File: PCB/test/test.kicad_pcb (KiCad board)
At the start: 2 copper layers, 64.1 x 42 mm, 174 parts, among them U1 STM32WBxx_QFN48, U2 USBLC6-2SC6, U3 LD3985M33R, U4 SFH_7072, X1 NX2016_32MHz, X2 NX2012_32K768Hz

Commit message: ajout alim TSU104
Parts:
- removed the ? at (159.2, 106.1)
- removed the ? at (162.4, 89.5)
- removed the ? at (165.3, 94.5)
- removed the ? at (170.0, 90.9)
- removed the ? at (156.3, 94.9)
- added ?: , , F.Cu at (167.5, 89.2)
- added ?: , , F.Cu at (162.3, 105.3)
- moved R11 4.28 mm to (162.2, 94.5), turned to -90 degrees
- moved R5 3.90 mm to (159.5, 89.6)
- moved ? 2.38 mm to (163.8, 101.0)
- moved ? 2.24 mm to (159.2, 105.8)
- moved R6 1.85 mm to (161.3, 90.6)
- moved ? 1.30 mm to (167.5, 90.9)
- moved C42 1.21 mm to (159.7, 93.5)
- moved R12 1.12 mm to (174.7, 101.6), turned to 0 degrees
- moved C43 0.85 mm to (161.3, 92.0)
- moved ? 0.11 mm to (156.3, 109.0)
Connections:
- TSU1 pad 1: (no net) -> Net-(C43-Pad2)
- TSU1 pad 11: (no net) -> GND
- TSU1 pad 2: (no net) -> Net-(C43-Pad1)
- TSU1 pad 3: (no net) -> GND
- TSU1 pad 4: (no net) -> 3V3
- TSU1 pad 5: GND -> (no net)
- TSU1 pad 6: Net-(C43-Pad1) -> (no net)
- TSU1 pad 7: Net-(C43-Pad2) -> (no net)
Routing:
- net Net-(C43-Pad1): track 13.9 -> 19.2 mm
- net PA4: track 29.4 -> 33.4 mm
- net PA5: track 52.3 -> 53.9 mm
- net GND: track 13.1 -> 11.5 mm
- net 3V3: track 157.2 -> 156.1 mm, vias 12 -> 13

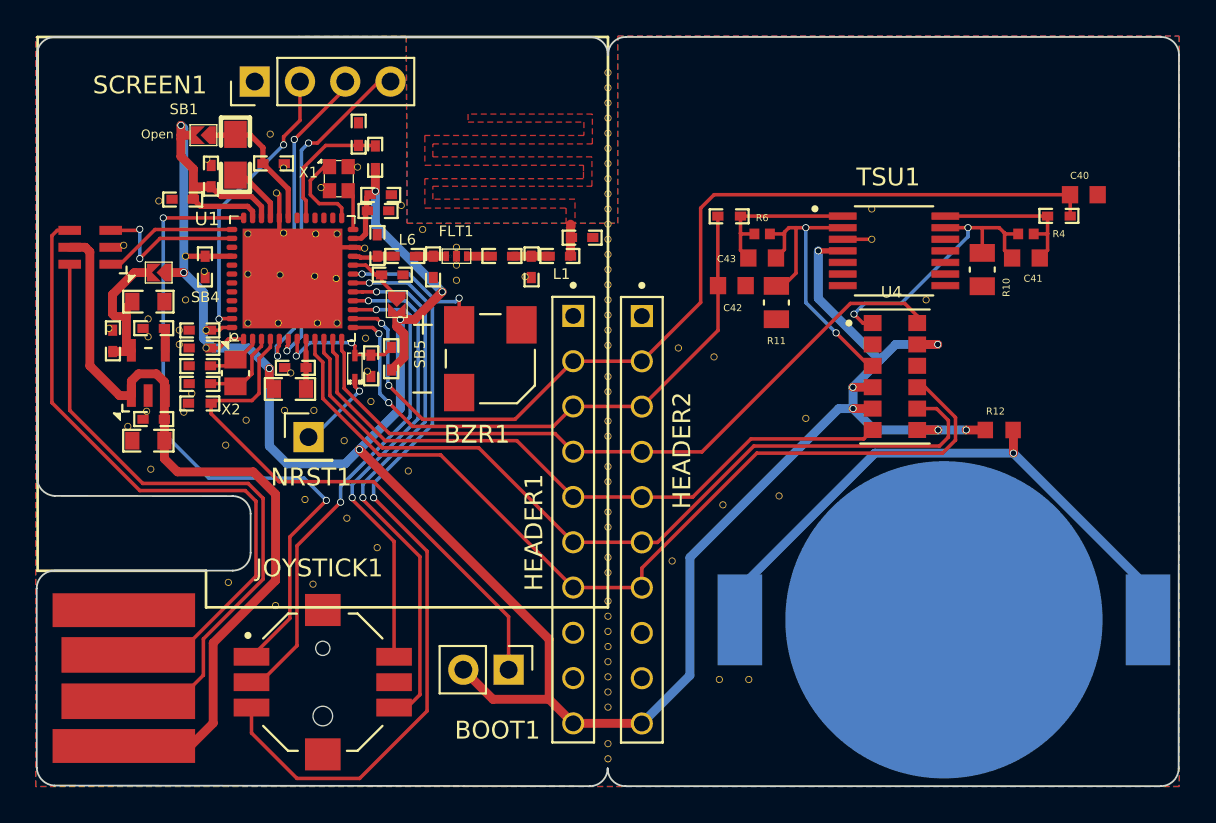
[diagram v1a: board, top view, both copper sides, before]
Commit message: ajout i2c
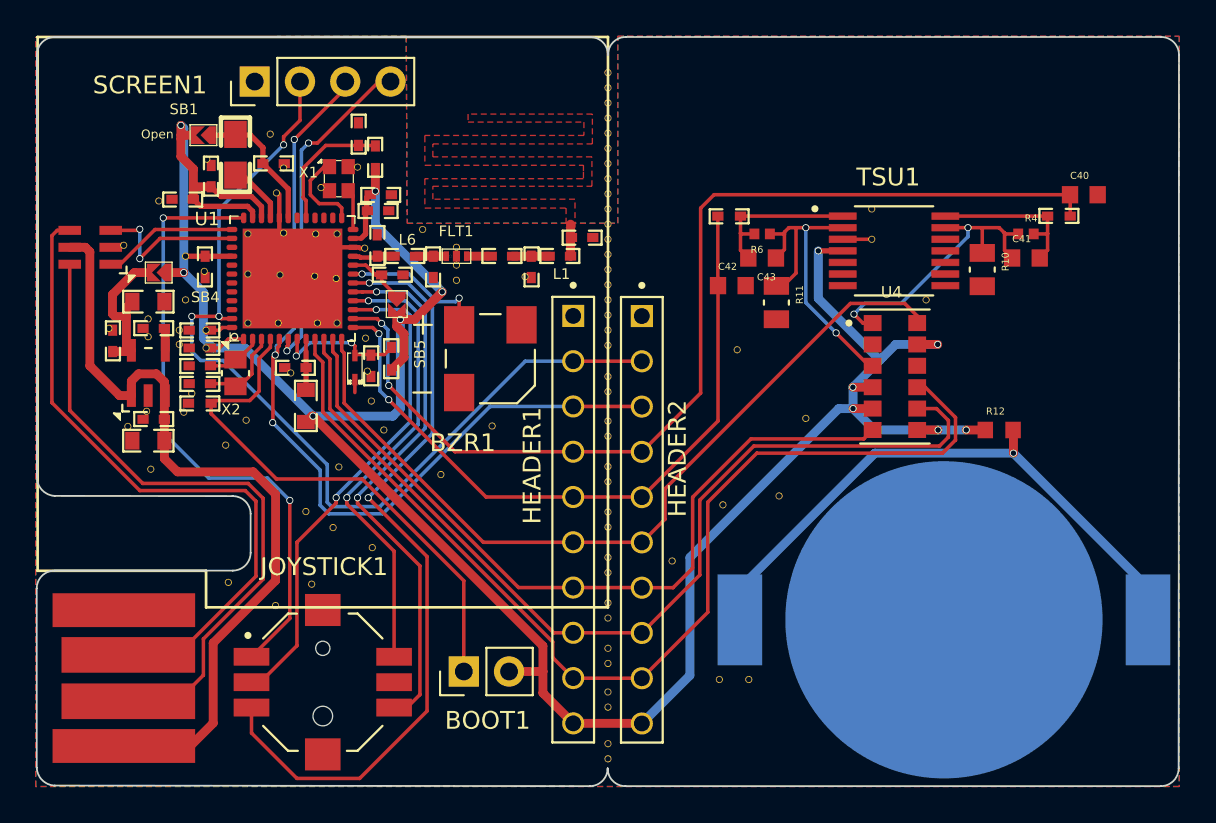
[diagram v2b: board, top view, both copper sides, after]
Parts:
- removed the ? at (137.9, 102.2)
- removed the ? at (136.2, 100.5)
- removed the ? at (152.7, 112.9)
- removed the ? at (141.1, 89.0)
- removed the ? at (134.6, 100.5)
- removed the ? at (152.7, 115.5)
- removed the ? at (141.5, 103.9)
- removed the ? at (156.7, 97.0)
- removed NRST1: Conn_01x01_Female, Connector_PinHeader_2.54mm:PinHeader_1x01_P2.54mm_Vertical
- added ?: , , F.Cu at (140.1, 101.6)
- added ?: , , F.Cu at (146.2, 101.4)
- added ?: , , F.Cu at (137.6, 103.7)
- added ?: , , F.Cu at (143.3, 104.1)
- moved BOOT1 2.52 mm to (144.6, 115.2), turned to 90 degrees
- moved ? 1.36 mm to (159.9, 97.1)
- moved L3 1.30 mm to (135.8, 100.2), turned to 90 degrees
- moved ? 0.94 mm to (137.3, 107.1)
- moved ? 0.68 mm to (135.8, 106.2)
- moved ? 0.28 mm to (139.5, 108.2)
- moved ? 0.10 mm to (152.7, 114.7)
- moved ? 0.10 mm to (152.7, 112.2)
- moved ? 0.10 mm to (152.7, 111.3)
- moved ? 0.10 mm to (152.7, 113.8)
- moved ? 0.08 mm to (136.1, 110.2)
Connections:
- HEADER1 pad 2: PA5 -> I2C_SDA
- HEADER1 pad 3: PA4 -> I2C_SCL
- HEADER1 pad 4: PA3 -> PA5
- HEADER1 pad 5: PA2 -> PA4
- HEADER1 pad 6: PA1 -> PA3
- HEADER1 pad 7: PA0 -> PA2
- HEADER1 pad 8: unconnected-(HEADER1-Pad8) -> PA1
- HEADER1 pad 9: unconnected-(HEADER1-Pad9) -> PA0
- HEADER2 pad 2: PA5 -> I2C_SDA
- HEADER2 pad 3: PA4 -> I2C_SCL
- HEADER2 pad 4: PA3 -> PA5
- HEADER2 pad 5: PA2 -> PA4
- HEADER2 pad 6: PA1 -> PA3
- HEADER2 pad 7: PA0 -> PA2
- HEADER2 pad 8: unconnected-(HEADER2-Pad8) -> PA1
- HEADER2 pad 9: unconnected-(HEADER2-Pad9) -> PA0
- SCREEN1 pad 2: Net-(SCREEN1-Pad2) -> I2C_SDA
- SCREEN1 pad 3: Net-(SCREEN1-Pad3) -> I2C_SCL
- U1 pad 47: Net-(SCREEN1-Pad2) -> I2C_SDA
- U1 pad 5: Net-(SCREEN1-Pad3) -> I2C_SCL
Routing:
- net I2C_SDA: track 0.00 -> 52.8 mm, vias 0 -> 3
- net I2C_SCL: track 0.00 -> 48.3 mm, vias 0 -> 3
- net Net-(SCREEN1-Pad3): track 18.0 -> 0.00 mm, vias 2 -> 0
- net Net-(SCREEN1-Pad2): track 15.9 -> 0.00 mm, vias 2 -> 0
- net PA0: track 51.6 -> 59.7 mm
- net PA1: track 46.8 -> 53.9 mm
- net PA2: track 37.1 -> 44.1 mm
- net PA4: track 33.4 -> 39.5 mm
- net 3V3: track 156.1 -> 150.0 mm, vias 13 -> 12
- net PA3: track 40.6 -> 46.3 mm
- net PA5: track 53.9 -> 58.4 mm
- net NRST: track 4.68 -> 0.72 mm, vias 1 -> 0
- net PA10: track 37.8 -> 34.9 mm
- net Net-(BOOT1-Pad1): track 31.2 -> 29.9 mm

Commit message: ajout 4 trous
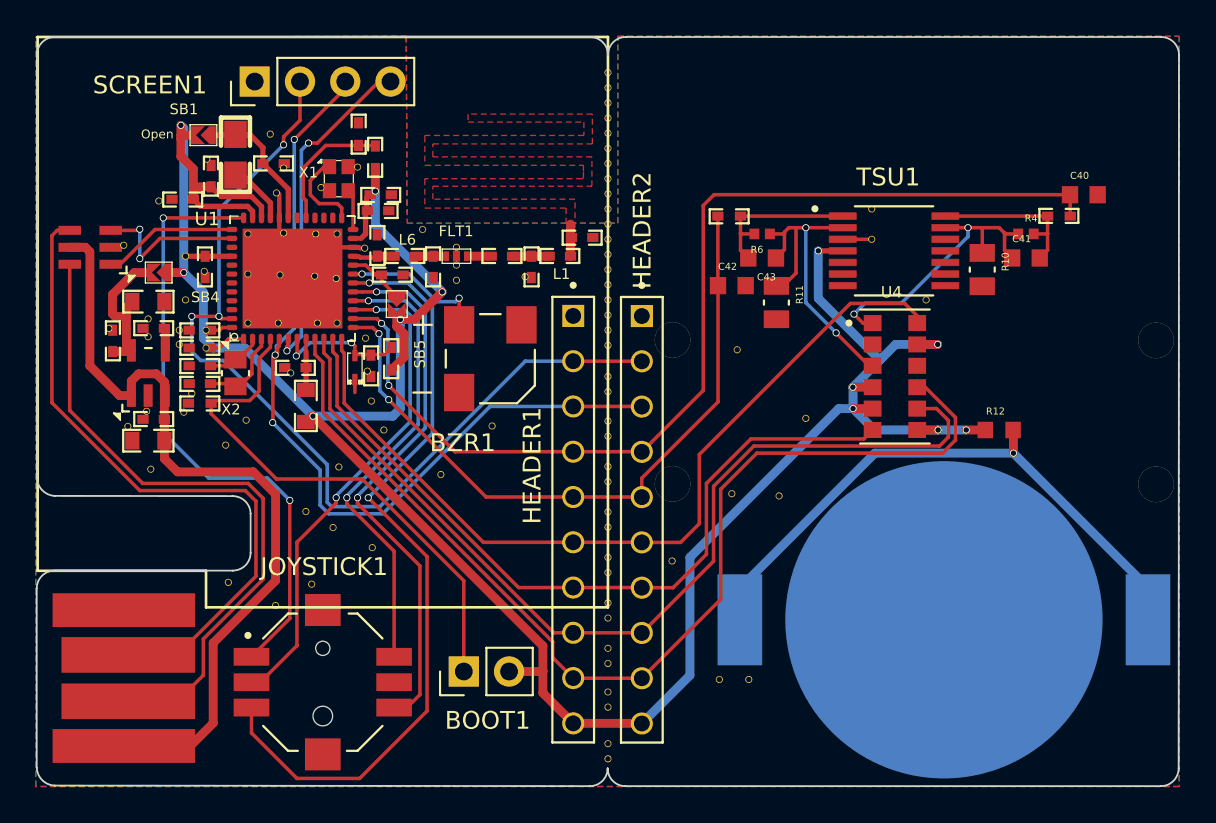
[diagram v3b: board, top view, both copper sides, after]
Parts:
- added ?: , , F.Cu at (183.4, 96.6)
- added ?: , , F.Cu at (156.3, 104.6)
- added ?: , , F.Cu at (156.3, 96.5)
- added ?: , , F.Cu at (183.4, 104.7)
- moved ? 0.80 mm to (159.7, 105.2)
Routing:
- net PA3: track 46.3 -> 47.6 mm

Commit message: améliorations pcb
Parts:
- added ?: , , F.Cu at (143.2, 109.8)
- added ?: , , F.Cu at (148.1, 119.2)
- added ?: , , F.Cu at (157.2, 95.1)
- added ?: , , F.Cu at (182.2, 85.1)
- added ?: , , F.Cu at (140.0, 90.0)
- added ?: , , F.Cu at (133.6, 118.3)
- added ?: , , F.Cu at (122.8, 82.2)
- added ?: , , F.Cu at (146.9, 108.6)
- added ?: , , F.Cu at (178.2, 90.7)
- added ?: , , F.Cu at (143.6, 97.9)
- added ?: , , F.Cu at (157.9, 119.2)
- added ?: , , F.Cu at (135.2, 91.8)
- added ?: , , F.Cu at (135.3, 95.6)
- added ?: , , F.Cu at (133.4, 91.7)
- added ?: , , F.Cu at (125.8, 83.7)
- added ?: , , F.Cu at (125.9, 89.6)
- added ?: , , F.Cu at (149.6, 120.3)
- added ?: , , F.Cu at (143.6, 101.1)
- added ?: , , F.Cu at (140.6, 87.8)
- added ?: , , F.Cu at (134.0, 83.0)
- added ?: , , F.Cu at (131.8, 118.3)
- added ?: , , F.Cu at (171.4, 82.7)
- added ?: , , F.Cu at (166.0, 101.4)
- added ?: , , F.Cu at (159.7, 94.8)
- added ?: , , F.Cu at (145.1, 103.5)
- added ?: , , F.Cu at (130.1, 102.4)
- added ?: , , F.Cu at (123.1, 102.8)
- added ?: , , F.Cu at (136.0, 102.2)
- added ?: , , F.Cu at (165.4, 103.7)
- added ?: , , F.Cu at (159.7, 100.1)
- added ?: , , F.Cu at (128.5, 83.5)
- added ?: , , F.Cu at (121.7, 101.4)
- added ?: , , F.Cu at (166.3, 98.1)
- added ?: , , F.Cu at (127.0, 97.5)
- added ?: , , F.Cu at (142.8, 118.3)
- added ?: , , F.Cu at (143.4, 112.3)
- added ?: , , F.Cu at (156.7, 83.5)
- added ?: , , F.Cu at (172.9, 100.5)
- added ?: , , F.Cu at (135.8, 94.3)
- added ?: , , F.Cu at (156.4, 87.7)
- added ?: , , F.Cu at (157.1, 106.3)
- added ?: , , F.Cu at (177.0, 99.4)
- added ?: , , F.Cu at (124.5, 104.3)
- added ?: , , F.Cu at (127.9, 86.7)
- added ?: , , F.Cu at (165.8, 85.3)
- added ?: , , F.Cu at (176.1, 93.2)
- added ?: , , F.Cu at (148.9, 111.2)
- added ?: , , F.Cu at (171.2, 98.0)
- added ?: , , F.Cu at (160.6, 101.3)
- added ?: , , F.Cu at (125.5, 87.5)
- added ?: , , F.Cu at (134.1, 102.6)
- added ?: , , F.Cu at (145.0, 120.0)
- added ?: , , F.Cu at (159.9, 85.7)
- added ?: , , F.Cu at (132.4, 91.7)
- added ?: , , F.Cu at (149.6, 90.2)
- added ?: , , F.Cu at (139.3, 84.7)
- added ?: , , F.Cu at (147.4, 99.5)
- added ?: , , F.Cu at (122.5, 88.0)
- added ?: , , F.Cu at (163.5, 98.5)
- added ?: , , F.Cu at (180.7, 99.5)
- added ?: , , F.Cu at (163.8, 82.4)
- added ?: , , F.Cu at (171.4, 95.8)
- added ?: , , F.Cu at (165.1, 97.0)
- added ?: , , F.Cu at (151.6, 90.1)
- added ?: , , F.Cu at (174.5, 96.5)
- added ?: , , F.Cu at (122.0, 104.0)
- added ?: , , F.Cu at (150.2, 92.8)
- added ?: , , F.Cu at (123.5, 85.6)
- added ?: , , F.Cu at (183.3, 118.9)
- added ?: , , F.Cu at (172.4, 85.4)
- added ?: , , F.Cu at (137.5, 94.4)
- added ?: , , F.Cu at (181.3, 90.7)
- added ?: , , F.Cu at (139.9, 113.0)
- added ?: , , F.Cu at (145.4, 111.3)
- added ?: , , F.Cu at (133.6, 90.6)
- added ?: , , F.Cu at (155.7, 91.2)
- added ?: , , F.Cu at (157.0, 103.0)
- added ?: , , F.Cu at (179.2, 81.9)
- added ?: , , F.Cu at (157.2, 99.0)
- added ?: , , F.Cu at (140.6, 86.3)
- added ?: , , F.Cu at (178.3, 95.9)
- added ?: , , F.Cu at (140.5, 118.5)
- added ?: , , F.Cu at (183.1, 107.5)
- added ?: , , F.Cu at (140.2, 90.8)
- added ?: , , F.Cu at (135.8, 105.0)
- added ?: , , F.Cu at (134.0, 94.3)
- added ?: , , F.Cu at (142.2, 92.8)
- added ?: , , F.Cu at (178.2, 86.7)
- added ?: , , F.Cu at (162.7, 96.9)
- added ?: , , F.Cu at (139.9, 110.8)
- added ?: , , F.Cu at (132.4, 94.3)
- added ?: , , F.Cu at (137.5, 91.8)
- added ?: , , F.Cu at (130.1, 101.3)
- moved ? 0.71 mm to (132.8, 101.6)
- moved ? 0.56 mm to (128.8, 99.5)
- moved ? 0.51 mm to (135.0, 87.1)
- moved ? 0.38 mm to (134.9, 90.6)
- moved ? 0.16 mm to (128.8, 100.5)
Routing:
- net 3V3: track 150.0 -> 155.7 mm, vias 12 -> 11
- net GND: track 11.5 -> 7.77 mm
- net Net-(SCREEN1-Pad4): track 18.9 -> 22.5 mm
- net I2C_SDA: track 52.8 -> 56.2 mm
- net I2C_SCL: track 48.3 -> 51.3 mm

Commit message: update pcb
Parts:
- removed the ? at (182.2, 85.1)
- removed the ? at (125.8, 101.4)
- removed the ? at (171.4, 82.7)
- removed the ? at (135.8, 106.2)
- removed the ? at (127.0, 103.8)
- removed the ? at (156.7, 83.5)
- removed the ? at (156.4, 87.7)
- removed the ? at (165.8, 85.3)
- removed the ? at (159.9, 85.7)
- removed the ? at (163.8, 82.4)
- removed the ? at (137.3, 107.1)
- removed the ? at (136.1, 110.2)
- removed the ? at (172.4, 85.4)
- removed the ? at (179.2, 81.9)
- removed the ? at (135.8, 105.0)
- removed the ? at (178.2, 86.7)
- removed C4: 10nF, Library:0402_CAP_NPOL
- added ?: , , F.Cu at (177.3, 87.5)
- added ?: , , F.Cu at (123.5, 100.5)
- added ?: , , F.Cu at (168.2, 83.5)
- added ?: , , F.Cu at (145.6, 90.4)
- added ?: , , F.Cu at (137.9, 108.7)
- added ?: , , F.Cu at (182.1, 83.6)
- added ?: , , F.Cu at (165.4, 87.3)
- added ?: , , F.Cu at (136.2, 106.6)
- added ?: , , F.Cu at (165.2, 80.5)
- added ?: , , F.Cu at (150.1, 92.9)
- added ?: , , F.Cu at (174.1, 83.7)
- added ?: , , F.Cu at (137.9, 110.1)
- added ?: , , F.Cu at (135.2, 105.2)
- added ?: , , F.Cu at (171.2, 87.2)
- moved C23 10.8 mm to (135.2, 109.0), turned to 180 degrees
- moved C24 10.2 mm to (134.9, 107.8), turned to 180 degrees
- moved ? 3.09 mm to (127.5, 104.7)
- moved ? 3.01 mm to (121.3, 98.4)
- moved C7 2.82 mm to (149.0, 92.5), turned to 90 degrees
- moved ? 2.60 mm to (145.4, 93.0)
- moved ? 2.60 mm to (147.6, 92.8)
- moved C6 2.60 mm to (145.8, 92.4)
- moved L1 2.60 mm to (147.4, 91.8)
- moved ? 2.35 mm to (125.5, 102.5)
- moved ? 0.52 mm to (139.8, 108.6)
- moved ? 0.08 mm to (151.7, 90.2)
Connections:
- C6 pad 1: Net-(C4-Pad2) -> Net-(C6-Pad1)
- FLT1 pad 3: Net-(C4-Pad1) -> Net-(C6-Pad1)
- L1 pad 1: Net-(C4-Pad2) -> Net-(C6-Pad1)
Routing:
- net PA10: track 34.9 -> 42.8 mm
- net /ANT: track 1.80 -> 6.51 mm
- net PA6: track 27.9 -> 31.7 mm
- net Net-(C4-Pad2): track 2.05 -> 0.00 mm
- net Net-(C6-Pad1): track 0.00 -> 1.90 mm
- net Net-(U2-Pad4): track 37.4 -> 35.9 mm
- net Net-(U2-Pad6): track 37.2 -> 35.7 mm
- net Net-(C4-Pad1): track 1.10 -> 0.00 mm
- net 5V_USB: track 44.9 -> 44.1 mm

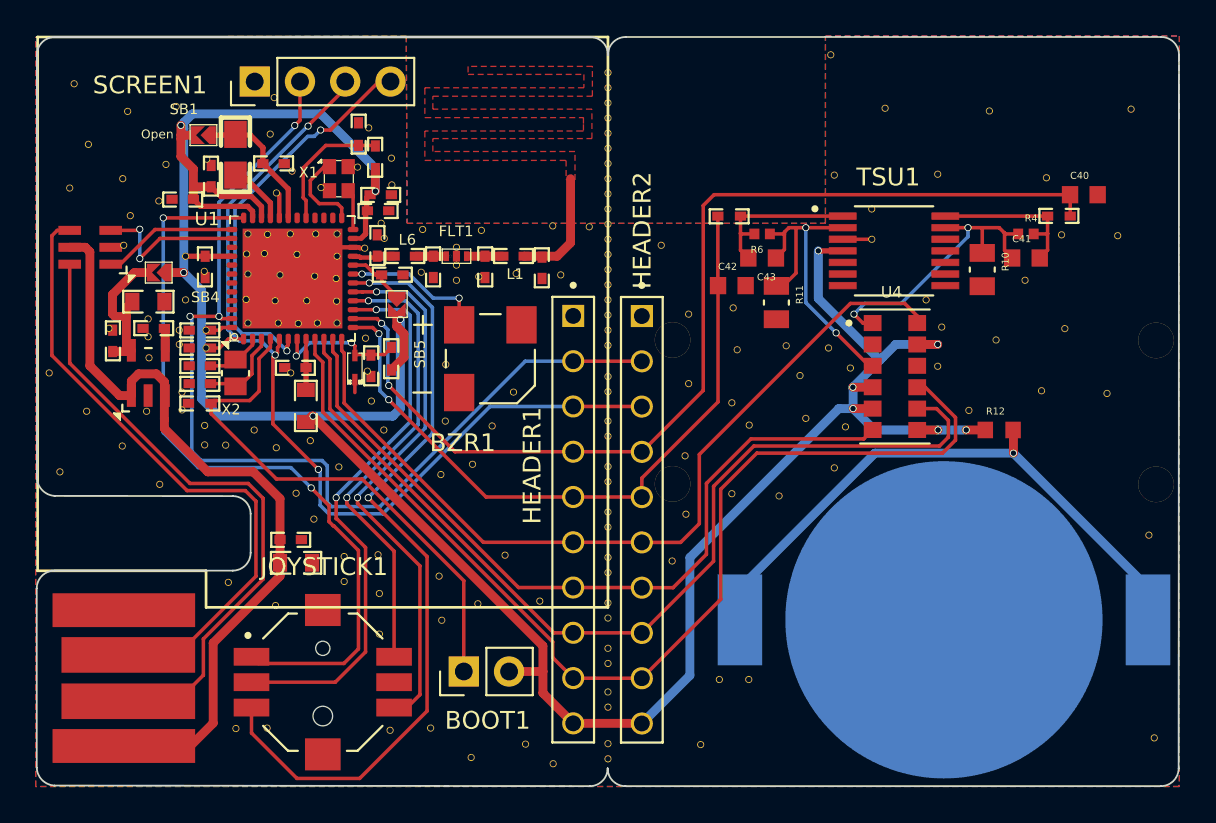
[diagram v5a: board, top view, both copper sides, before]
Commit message: changement cables USB vers transimpédance de 120 ohms
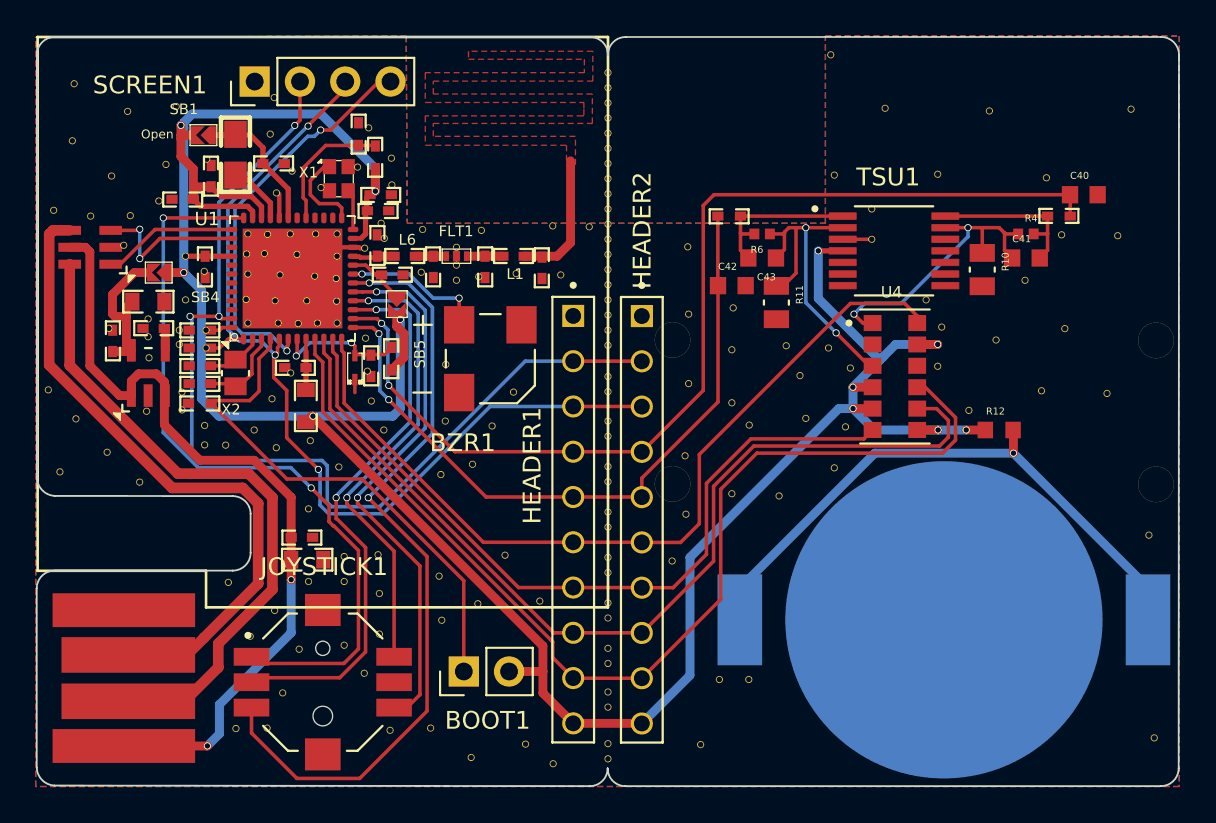
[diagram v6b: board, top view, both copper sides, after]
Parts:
- removed the ? at (134.1, 111.5)
- removed the ? at (135.2, 105.2)
- added ?: , , F.Cu at (134.4, 116.3)
- added ?: , , F.Cu at (137.9, 113.7)
- added ?: , , F.Cu at (135.9, 110.1)
- added ?: , , F.Cu at (133.8, 99.8)
- added ?: , , F.Cu at (134.0, 111.7)
- added ?: , , F.Cu at (132.6, 113.2)
- added ?: , , F.Cu at (135.4, 113.9)
- added ?: , , F.Cu at (139.0, 115.2)
- added ?: , , F.Cu at (124.8, 87.3)
- moved ? 2.77 mm to (123.7, 89.6)
- moved ? 1.54 mm to (121.6, 89.3)
- moved ? 1.49 mm to (157.2, 91.3)
- moved ? 1.13 mm to (126.4, 104.5)
- moved ? 0.95 mm to (121.3, 99.3)
- moved ? 0.92 mm to (122.7, 85.4)
- moved ? 0.92 mm to (124.6, 102.8)
- moved ? 0.74 mm to (122.8, 101.0)
- moved C23 0.65 mm to (135.8, 108.9)
- moved ? 0.65 mm to (135.9, 106.0)
- moved C24 0.64 mm to (135.5, 107.6)
- moved ? 0.30 mm to (159.7, 97.1)
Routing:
- net 5V_USB: track 44.1 -> 45.5 mm, vias 0 -> 2
- net Net-(U2-Pad4): track 35.9 -> 37.0 mm
- net Net-(U2-Pad6): track 35.7 -> 36.7 mm
- net /ANT: track 6.51 -> 7.51 mm
